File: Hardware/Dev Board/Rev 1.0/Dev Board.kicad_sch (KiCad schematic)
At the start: 50 parts, among them J1 VBAT, J2 Communication, J3 Panel, J4 6502 Card Connector, J5 6502 Bus, J6 USB Host, J7 USB Host, J8 RJ45_LED, J9 Ethernet, SW1 Run/Stop, SW2 Step, SW3 Clock, SW4 Reset, U1 74HCT245, U2 74HCT245, U3 74HCT245, U4 Teensy4.1, U5 74LVC245, U6 74HCT245, U7 74LVC245, U8 74LVC1G04

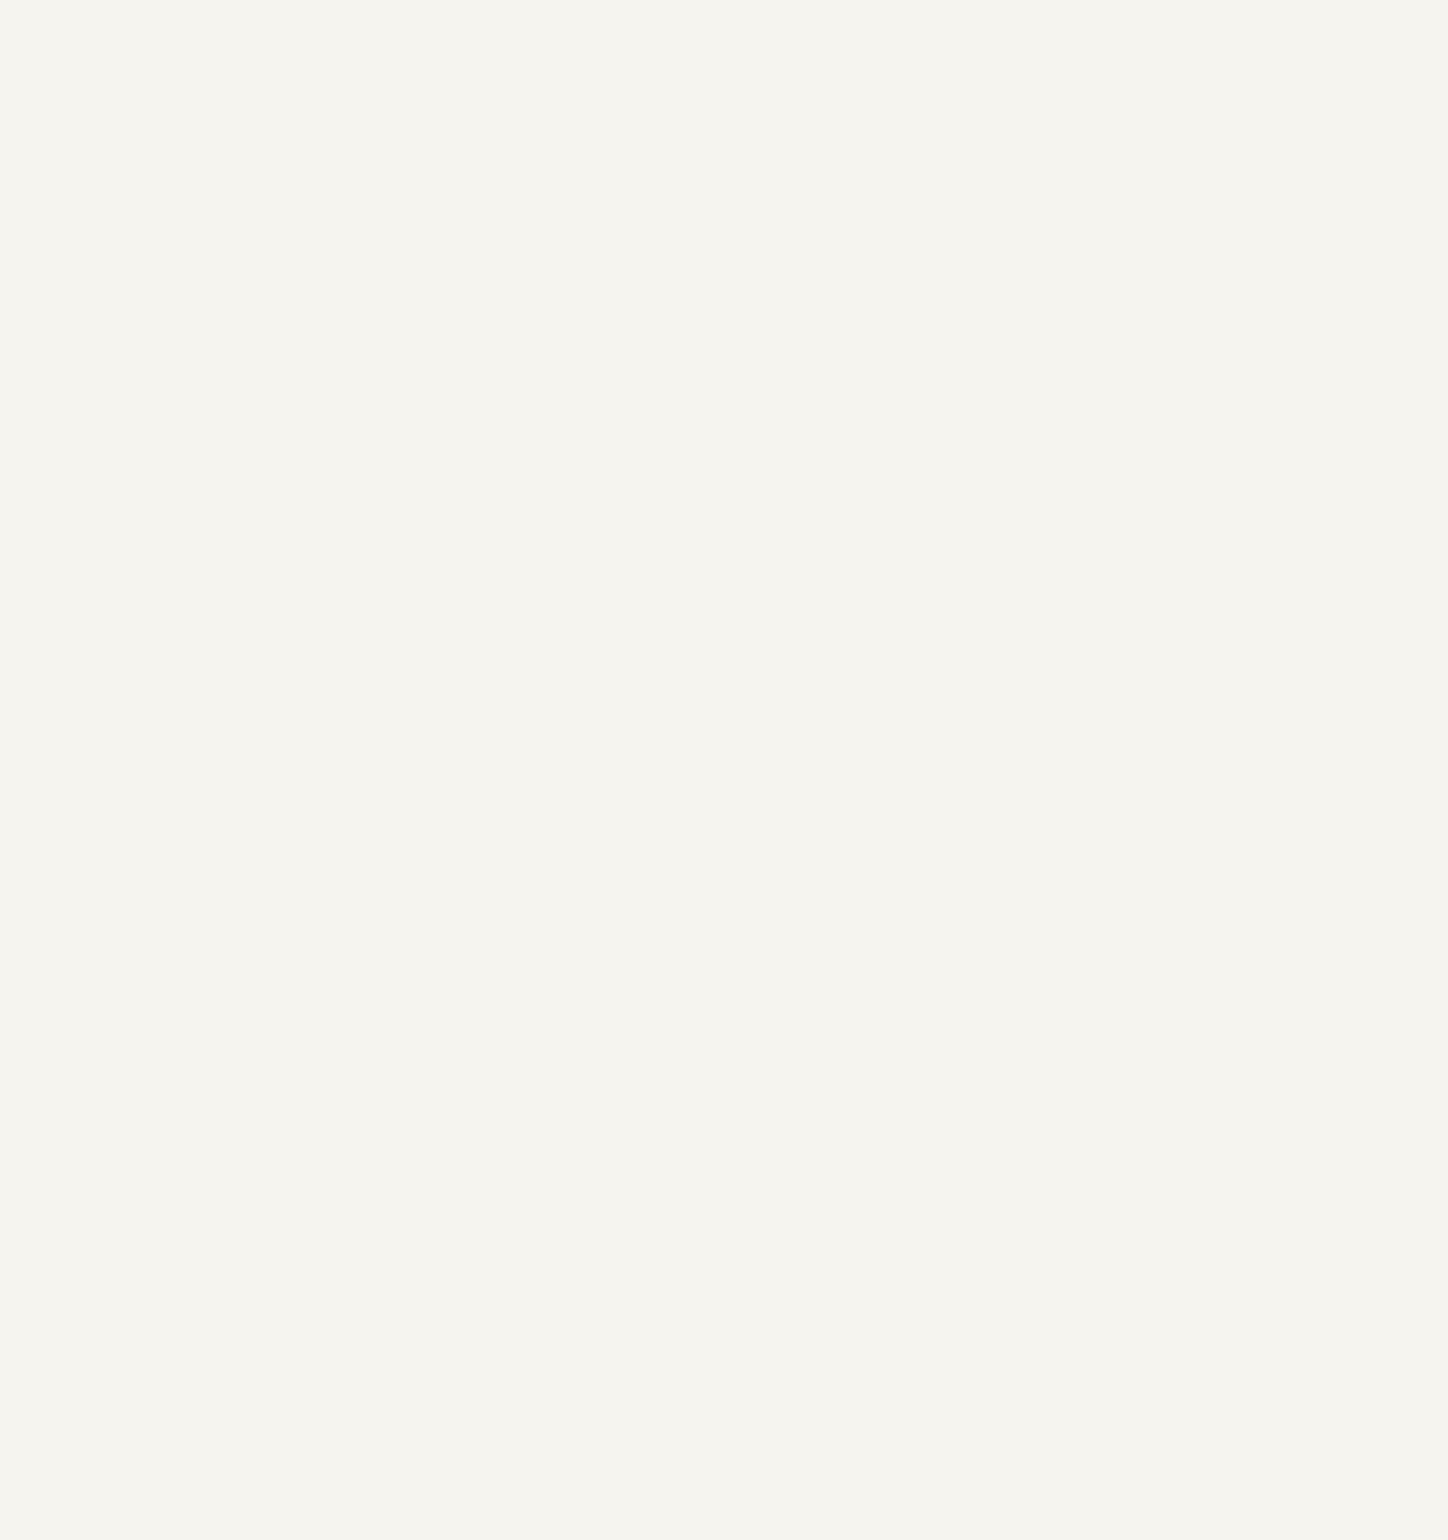
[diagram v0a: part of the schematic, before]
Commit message: Remove Teensy Card
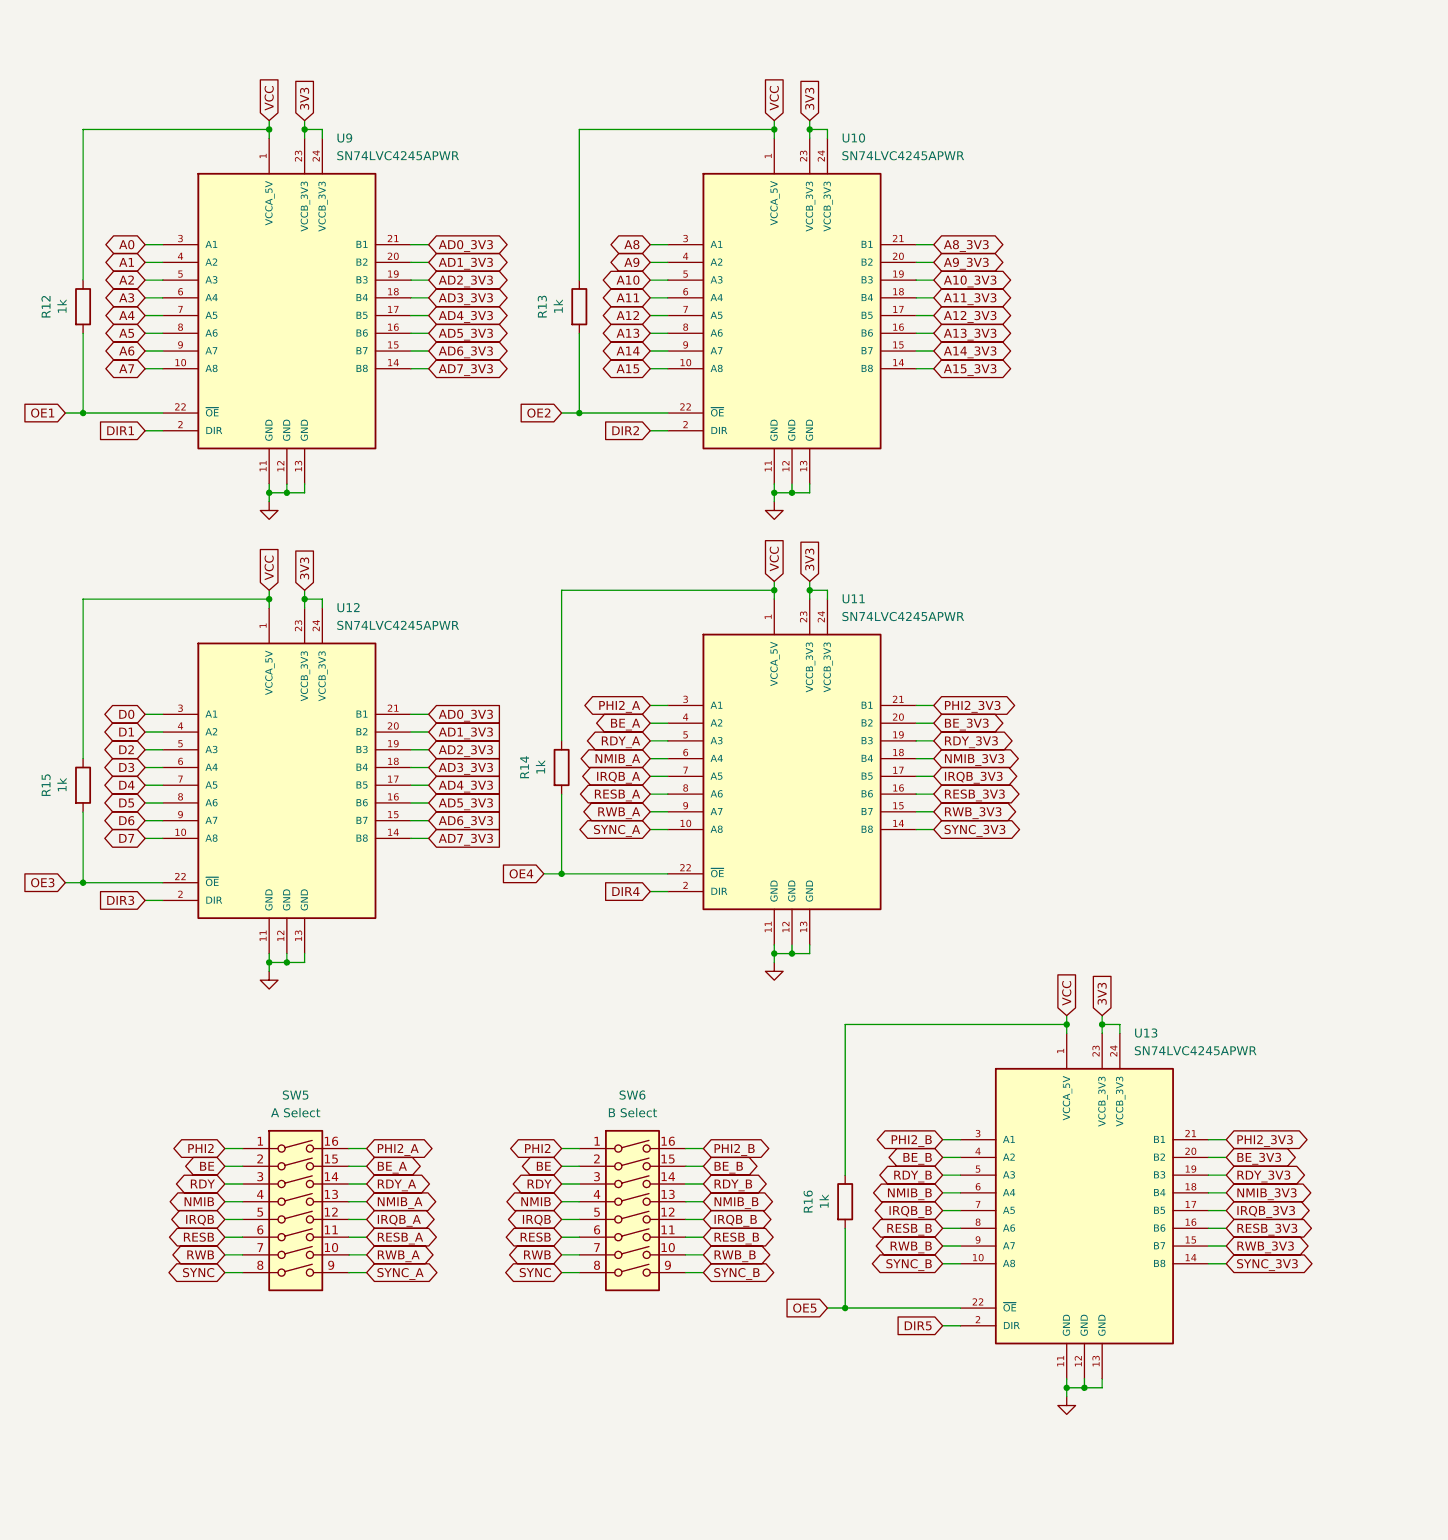
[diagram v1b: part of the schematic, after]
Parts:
- added R12, R13, R14, R15, R16: 1k, Resistor_SMD:R_0805_2012Metric, symbol Device:R
- added SW5: A Select, 6502 Parts:DS01C-254-L-08BE, symbol Switch:SW_DIP_x08
- added SW6: B Select, 6502 Parts:DS01C-254-L-08BE, symbol Switch:SW_DIP_x08
- added U10, U11, U12, U13, U9: SN74LVC4245APWR, Package_SO:TSSOP-24_4.4x7.8mm_P0.65mm, symbol 6502 Parts:SN74LVC4245APWR
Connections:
- net 3V3: now also U10.23 (VCCB_3V3), U10.24 (VCCB_3V3), U11.23 (VCCB_3V3), U11.24 (VCCB_3V3), U12.23 (VCCB_3V3), U12.24 (VCCB_3V3), U13.23 (VCCB_3V3), U13.24 (VCCB_3V3), U9.23 (VCCB_3V3), U9.24 (VCCB_3V3)
- net A0: now also U9.3 (A1)
- net A1: now also U9.4 (A2)
- net A10: now also U10.5 (A3)
- net A10_3V3: now also U10.19 (B3)
- net A11: now also U10.6 (A4)
- net A11_3V3: now also U10.18 (B4)
- net A12: now also U10.7 (A5)
- net A12_3V3: now also U10.17 (B5)
- net A13: now also U10.8 (A6)
- net A13_3V3: now also U10.16 (B6)
- net A14: now also U10.9 (A7)
- net A14_3V3: now also U10.15 (B7)
- net A15: now also U10.10 (A8)
- net A15_3V3: now also U10.14 (B8)
- net A2: now also U9.5 (A3)
- net A3: now also U9.6 (A4)
- net A4: now also U9.7 (A5)
- net A5: now also U9.8 (A6)
- net A6: now also U9.9 (A7)
- net A7: now also U9.10 (A8)
- net A8: now also U10.3 (A1)
- net A8_3V3: now also U10.21 (B1)
- net A9: now also U10.4 (A2)
- net A9_3V3: now also U10.20 (B2)
- net BE: now also SW5.2, SW6.2
- net BE_3V3: now also U11.20 (B2), U13.20 (B2)
- net D0: now also U12.3 (A1)
- net D1: now also U12.4 (A2)
- net D2: now also U12.5 (A3)
- net D3: now also U12.6 (A4)
- net D4: now also U12.7 (A5)
- net D5: now also U12.8 (A6)
- net D6: now also U12.9 (A7)
- net D7: now also U12.10 (A8)
- net GND: now also U10.11 (GND), U10.12 (GND), U10.13 (GND), U11.11 (GND), U11.12 (GND), U11.13 (GND), U12.11 (GND), U12.12 (GND), U12.13 (GND), U13.11 (GND), U13.12 (GND), U13.13 (GND), U9.11 (GND), U9.12 (GND), U9.13 (GND)
- net IRQB: now also SW5.5, SW6.5
- net IRQB_3V3: now also U11.17 (B5), U13.17 (B5)
- net NMIB: now also SW5.4, SW6.4
- net NMIB_3V3: now also U11.18 (B4), U13.18 (B4)
- net PHI2: now also SW5.1, SW6.1
- net PHI2_3V3: now also U11.21 (B1), U13.21 (B1)
- net RDY: now also SW5.3, SW6.3
- net RDY_3V3: now also U11.19 (B3), U13.19 (B3)
- net RESB: now also SW5.6, SW6.6
- net RESB_3V3: now also U11.16 (B6), U13.16 (B6)
- net RWB: now also SW5.7, SW6.7
- net RWB_3V3: now also U11.15 (B7), U13.15 (B7)
- net SYNC: now also SW5.8, SW6.8
- net SYNC_3V3: now also U11.14 (B8), U13.14 (B8)
- net VCC: now also R12.1, R13.1, R14.1, R15.1, R16.1, U10.1 (VCCA_5V), U11.1 (VCCA_5V), U12.1 (VCCA_5V), U13.1 (VCCA_5V), U9.1 (VCCA_5V)
- new net AD0_3V3: U12.21 (B1), U9.21 (B1)
- new net AD1_3V3: U12.20 (B2), U9.20 (B2)
- new net AD2_3V3: U12.19 (B3), U9.19 (B3)
- new net AD3_3V3: U12.18 (B4), U9.18 (B4)
- new net AD4_3V3: U12.17 (B5), U9.17 (B5)
- new net AD5_3V3: U12.16 (B6), U9.16 (B6)
- new net AD6_3V3: U12.15 (B7), U9.15 (B7)
- new net AD7_3V3: U12.14 (B8), U9.14 (B8)
- new net BE_A: SW5.15, U11.4 (A2)
- new net BE_B: SW6.15, U13.4 (A2)
- new net DIR1: U9.2 (DIR)
- new net DIR2: U10.2 (DIR)
- new net DIR3: U12.2 (DIR)
- new net DIR4: U11.2 (DIR)
- new net DIR5: U13.2 (DIR)
- new net IRQB_A: SW5.12, U11.7 (A5)
- new net IRQB_B: SW6.12, U13.7 (A5)
- new net NMIB_A: SW5.13, U11.6 (A4)
- new net NMIB_B: SW6.13, U13.6 (A4)
- new net OE1: R12.2, U9.22 (~{OE})
- new net OE2: R13.2, U10.22 (~{OE})
- new net OE3: R15.2, U12.22 (~{OE})
- new net OE4: R14.2, U11.22 (~{OE})
- new net OE5: R16.2, U13.22 (~{OE})
- new net PHI2_A: SW5.16, U11.3 (A1)
- new net PHI2_B: SW6.16, U13.3 (A1)
- new net RDY_A: SW5.14, U11.5 (A3)
- new net RDY_B: SW6.14, U13.5 (A3)
- new net RESB_A: SW5.11, U11.8 (A6)
- new net RESB_B: SW6.11, U13.8 (A6)
- new net RWB_A: SW5.10, U11.9 (A7)
- new net RWB_B: SW6.10, U13.9 (A7)
- new net SYNC_A: SW5.9, U11.10 (A8)
- new net SYNC_B: SW6.9, U13.10 (A8)

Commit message: Switch to 74LVC4245s
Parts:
- removed C11, C12: 100nF, Capacitor_SMD:C_0805_2012Metric, symbol Device:C
- removed R12, R13, R14, R15, R16: 1k, Resistor_SMD:R_0805_2012Metric, symbol Device:R
- removed SW5: A Select, 6502 Parts:DS01C-254-L-08BE, symbol Switch:SW_DIP_x08
- removed SW6: B Select, 6502 Parts:DS01C-254-L-08BE, symbol Switch:SW_DIP_x08
- removed U1, U2, U3, U6: 74HCT245, Package_SO:TSSOP-20_4.4x6.5mm_P0.65mm, symbol 74xx:74HC245
- removed U11, U13: SN74LVC4245APWR, Package_SO:TSSOP-24_4.4x7.8mm_P0.65mm, symbol 6502 Parts:SN74LVC4245APWR
- removed U5, U7: 74LVC245, Package_SO:TSSOP-20_4.4x6.5mm_P0.65mm, symbol 74xx:74HC245
- removed U8: 74LVC1G04, Package_TO_SOT_SMD:SOT-23-5_HandSoldering, symbol 74xGxx:74LVC1G04
- added U1, U2: SN74LVC4245APWR, Package_SO:TSSOP-24_4.4x7.8mm_P0.65mm, symbol 6502 Parts:SN74LVC4245APWR
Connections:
- net DIR1 is gone; now on net GND: U9.2 (DIR)
- net DIR2 is gone; now on net GND: U10.2 (DIR)
- net DIR3 is gone; now on net RWB: U12.2 (DIR)
- net OE1 is gone; now on net GND: U9.22 (~{OE})
- net OE2 is gone; now on net GND: U10.22 (~{OE})
- net OE3 is gone; now on net GND: U12.22 (~{OE})
- net 3V3: now also U1.23 (VCCB_3V3), U1.24 (VCCB_3V3), U2.23 (VCCB_3V3), U2.24 (VCCB_3V3); no longer C10.1, C9.2
- net A0_3V3: now also U9.21 (B1)
- net A1_3V3: now also U9.20 (B2)
- net A2_3V3: now also U9.19 (B3)
- net A3_3V3: now also U9.18 (B4)
- net A4_3V3: now also U9.17 (B5)
- net A5_3V3: now also U9.16 (B6)
- net A6_3V3: now also U9.15 (B7)
- net A7_3V3: now also U9.14 (B8)
- net BE: now also U2.6 (A4)
- net BE_3V3: now also U2.18 (B4)
- net D0_3V3: now also U12.21 (B1)
- net D1_3V3: now also U12.20 (B2)
- net D2_3V3: now also U12.19 (B3)
- net D3_3V3: now also U12.18 (B4)
- net D4_3V3: now also U12.17 (B5)
- net D5_3V3: now also U12.16 (B6)
- net D6_3V3: now also U12.15 (B7)
- net D7_3V3: now also U12.14 (B8)
- net EXP0: now also U2.7 (A5)
- net EXP0_3V3: now also U2.17 (B5)
- net GND: now also U1.11 (GND), U1.12 (GND), U1.13 (GND), U1.14 (B8), U1.15 (B7), U1.16 (B6), U1.17 (B5), U1.2 (DIR), U1.22 (~{OE}), U2.10 (A8), U2.11 (GND), U2.12 (GND), U2.13 (GND), U2.22 (~{OE}), U2.8 (A6), U2.9 (A7)
- net IRQB: now also U2.3 (A1)
- net IRQB_3V3: now also U2.21 (B1)
- net NMIB: now also U2.4 (A2)
- net NMIB_3V3: now also U2.20 (B2)
- net PHI2: now also U1.3 (A1)
- net PHI2_3V3: now also U1.21 (B1)
- net RDY: now also U2.5 (A3)
- net RDY_3V3: now also U2.19 (B3)
- net RESB: now also U1.4 (A2)
- net RESB_3V3: now also U1.20 (B2)
- net RWB: now also U1.5 (A3)
- net RWB_3V3: now also U1.19 (B3)
- net SYNC: now also U1.6 (A4)
- net SYNC_3V3: now also U1.18 (B4)
- net VCC: now also C10.1, C9.2, U1.1 (VCCA_5V), U2.1 (VCCA_5V), U2.2 (DIR)
- removed net AD0_3V3: U12.21 (B1), U9.21 (B1)
- removed net AD1_3V3: U12.20 (B2), U9.20 (B2)
- removed net AD2_3V3: U12.19 (B3), U9.19 (B3)
- removed net AD3_3V3: U12.18 (B4), U9.18 (B4)
- removed net AD4_3V3: U12.17 (B5), U9.17 (B5)
- removed net AD5_3V3: U12.16 (B6), U9.16 (B6)
- removed net AD6_3V3: U12.15 (B7), U9.15 (B7)
- removed net AD7_3V3: U12.14 (B8), U9.14 (B8)
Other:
- moved on the sheet: J2, J3, JP1, R1, R2, R3, R4, R5, U10, U12, U9

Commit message: Dev Board Layout
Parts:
- removed C10, C9: 100nF, Capacitor_SMD:C_0805_2012Metric, symbol Device:C
- J2: value Communication -> COM
- J3: value Panel -> PANEL
- J7: value USB Host -> USB HOST
- J8: symbol Connector:RJ45_LED -> Connector:RJ45_LED_Shielded
- J9: value Ethernet -> ETHERNET
- renumbered U9 to U1, U10 to U2, U1 to U3, U12 to U5, U2 to U6
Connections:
- net GND: now also J8.SH

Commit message: Housekeeping
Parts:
- removed H1, H2, H3, H4: MountingHole, MountingHole:MountingHole_3.2mm_M3, symbol Mechanical:MountingHole

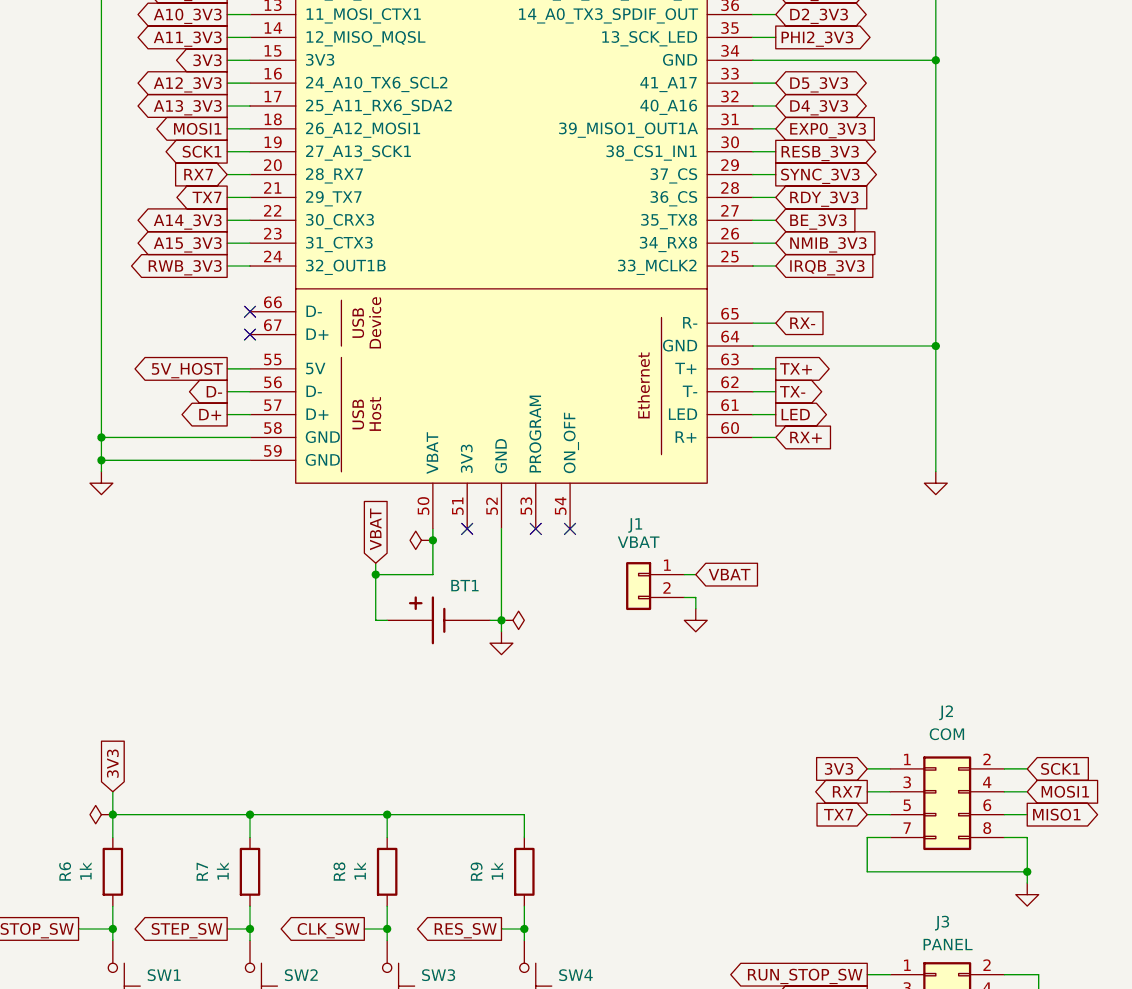
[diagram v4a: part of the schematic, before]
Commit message: Add SPI header to Dev Board
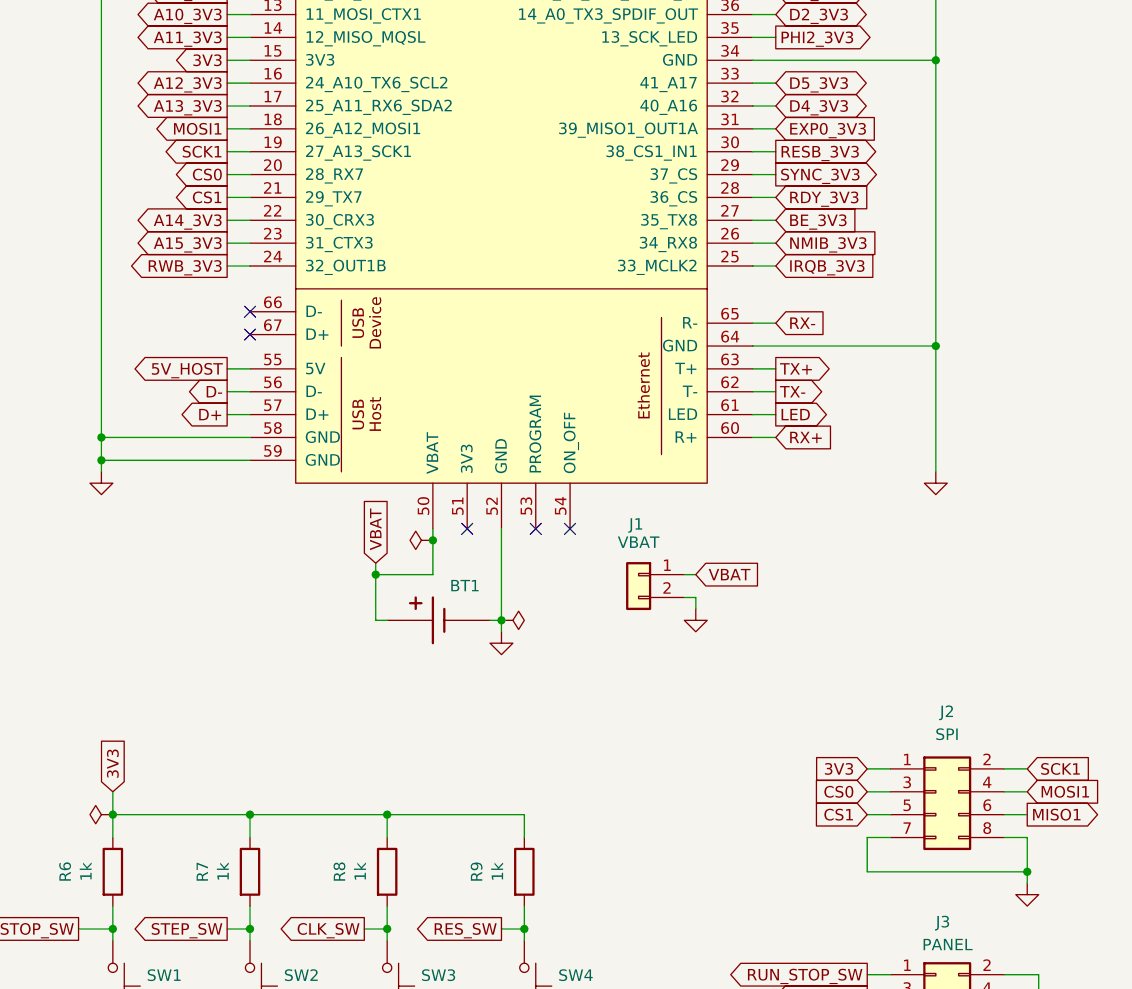
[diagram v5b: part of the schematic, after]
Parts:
- J2: value COM -> SPI
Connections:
- net RX7 renamed CS0
- net TX7 renamed CS1
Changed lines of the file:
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@@
 		)
 	)
-	(global_label "TX7"
+	(global_label "CS1"
 		(shape input)
 		(at 363.22 154.94 180)
@@
 		)
 		(property "Intersheetrefs" "${INTERSHEET_REFS}"
-			(at 356.8482 154.94 0)
+			(at 356.5458 154.94 0)
 			(effects
 				(font
@@
 		)
 	)
-	(global_label "RX7"
-		(shape output)
+	(global_label "CS0"
+		(shape input)
 		(at 363.22 152.4 180)
 		(fields_autoplaced yes)
@@
 		)
 	)
-	(global_label "TX7"
+	(global_label "CS1"
 		(shape output)
 		(at 292.1 86.36 180)
@@
 		)
 		(property "Intersheetrefs" "${INTERSHEET_REFS}"
-			(at 285.7282 86.36 0)
+			(at 285.4258 86.36 0)
 			(effects
 				(font
@@
 		)
 	)
-	(global_label "RX7"
-		(shape input)
+	(global_label "CS0"
+		(shape output)
 		(at 292.1 83.82 180)
 		(fields_autoplaced yes)
@@
 			)
 		)
-		(property "Value" "COM"
+		(property "Value" "SPI"
 			(at 372.11 146.05 0)
 			(effects
